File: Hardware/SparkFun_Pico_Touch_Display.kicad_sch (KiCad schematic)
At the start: 41 parts, among them J1 Conn_01x20, J2 Conn_01x20, J3 Conn_02x10_SMD_RA, J4 Conn_1x21_FPC, J5 Qwiic_Vertical, J6 microSD, Q1 RE1C002UNTCL, SW1 SMD_4.6x2.8mm_h2.5mm, U1 2" LCD-TFT 240x320

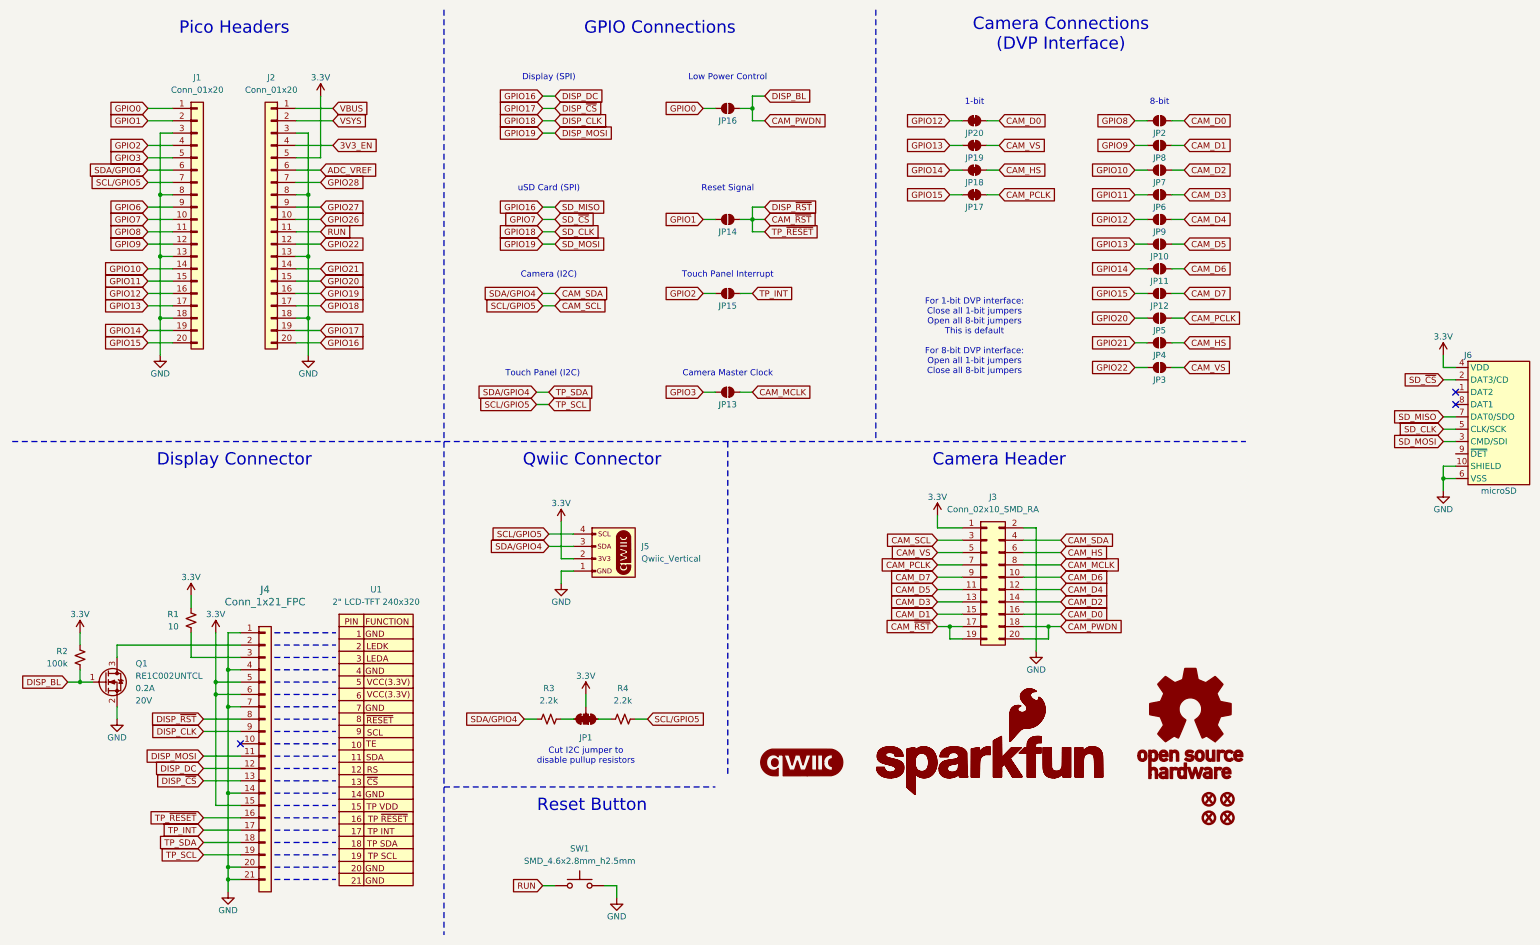
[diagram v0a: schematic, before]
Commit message: Clean up design
Finish routing
Add power LED
Move all schematic elements inside frame
Update display 3D model
Stitch together GND pours
Add measures
Fill out sheet info
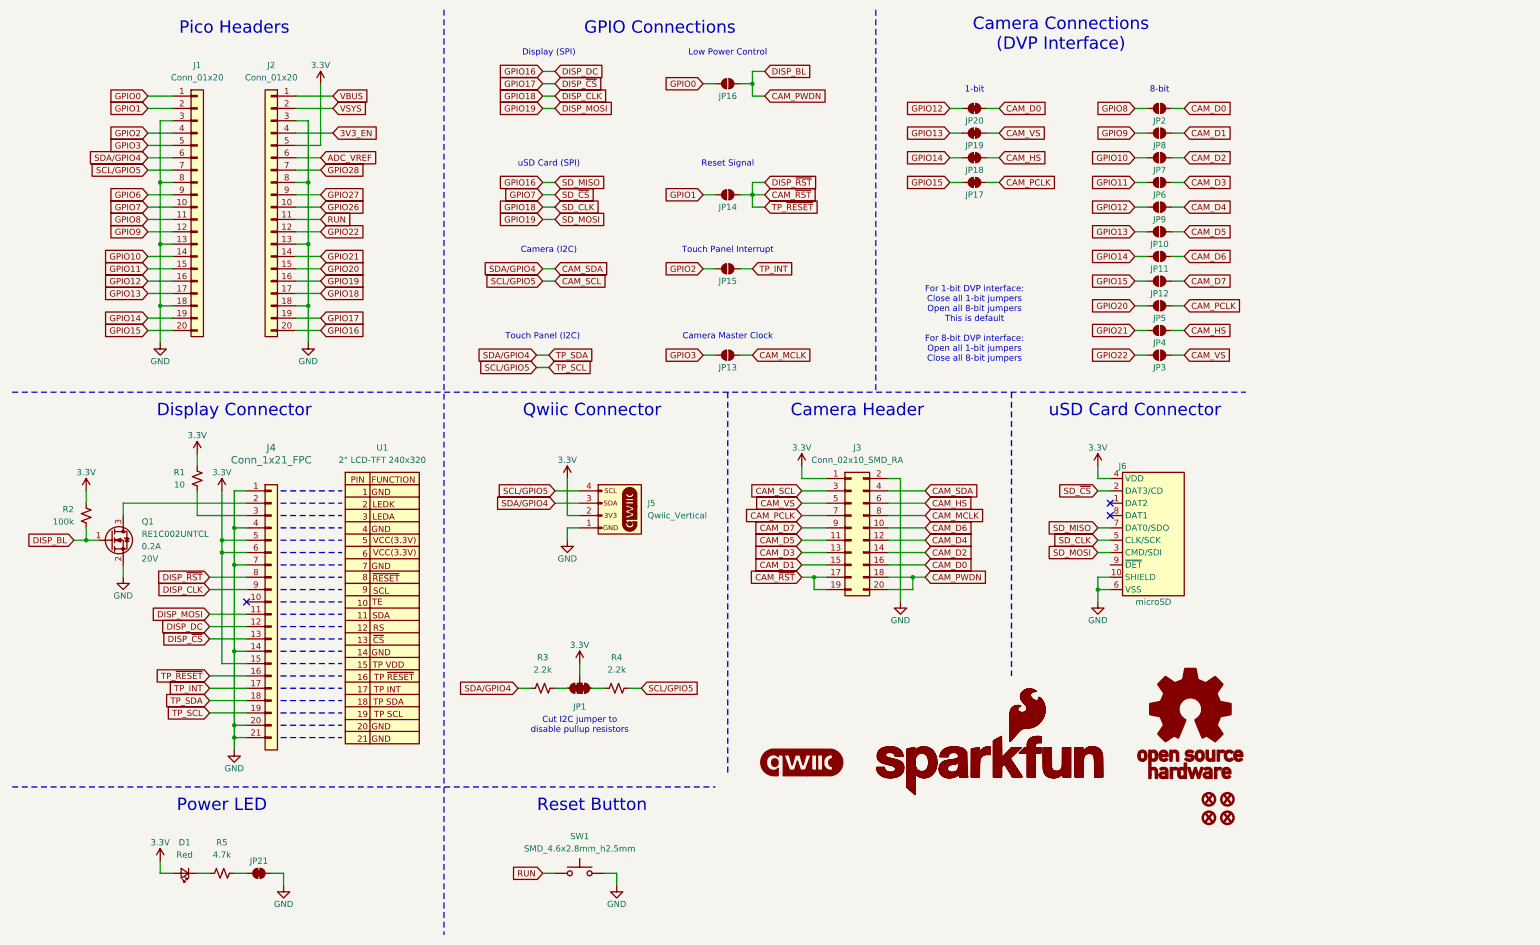
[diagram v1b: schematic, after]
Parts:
- added D1: Red, SparkFun-LED:LED_0603_1608Metric_Red, symbol SparkFun-LED:LED_Red_0603
- added JP21: ~, SparkFun-Jumper:Jumper_2_NC_Trace, symbol SparkFun-Jumper:SolderJumper_2_Bridged
- added R5: 4.7k, SparkFun-Resistor:R_0603_1608Metric, symbol SparkFun-Resistor:4.7k_0603
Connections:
- net 3.3V: now also D1.2 (A)
- net GND: now also JP21.2 (B)
- new net: D1.1 (K), R5.2
- new net: JP21.1 (A), R5.1
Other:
- note added: "Power LED"
- note added: "uSD Card Connector"
- company: SparkFun -> SparkFunElectronics
- title: SparkFun Product (Qwiic) -> SparkFun Pico Touch Display
- moved on the sheet: J1, J2, J3, J4, J5, J6, JP1, JP10, JP11, JP12, JP13, JP14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

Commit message: Design review updates
Rename jumpers to match silk
Nudge traces to provide more isolation of I2C traces
Add 10uF capacitor for uSD card
Fix acid trap
Rename MISO/MOSI to POCI/PICO
Increase 3.3V trace width
Change to 2 layer
Update ordering notes
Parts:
- added C1: 10uF, SparkFun-Capacitor:C_0603_1608Metric, symbol SparkFun-Capacitor:10uF_0603_6.3V_20%
- JP1: value ~ -> I2C
- JP10: value ~ -> 8-BIT-D5
- JP11: value ~ -> 8-BIT-D6
- JP12: value ~ -> 8-BIT-D7
- JP13: value ~ -> MCLK
- JP14: value ~ -> ~{RST}
- JP15: value ~ -> TP_INT
- JP16: value ~ -> LP
- JP17: value ~ -> 1-BIT-PCLK
- JP18: value ~ -> 1-BIT-HS
- JP19: value ~ -> 1-BIT-VS
- JP2: value ~ -> 8-BIT-D0
- JP20: value ~ -> 1-BIT-D0
- JP21: value ~ -> PWR
- JP3: value ~ -> 8-BIT-VS
- JP4: value ~ -> 8-BIT-HS
- JP5: value ~ -> 8-BIT-PCLK
- JP6: value ~ -> 8-BIT-D3
- JP7: value ~ -> 8-BIT-D2
- JP8: value ~ -> 8-BIT-D1
- JP9: value ~ -> 8-BIT-D4
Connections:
- net 3.3V: now also C1.1
- net GND: now also C1.2
- net DISP_MOSI renamed DISP_PICO
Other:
- note added: "Cut PWR jumper to disable power LED"
- moved on the sheet: J6

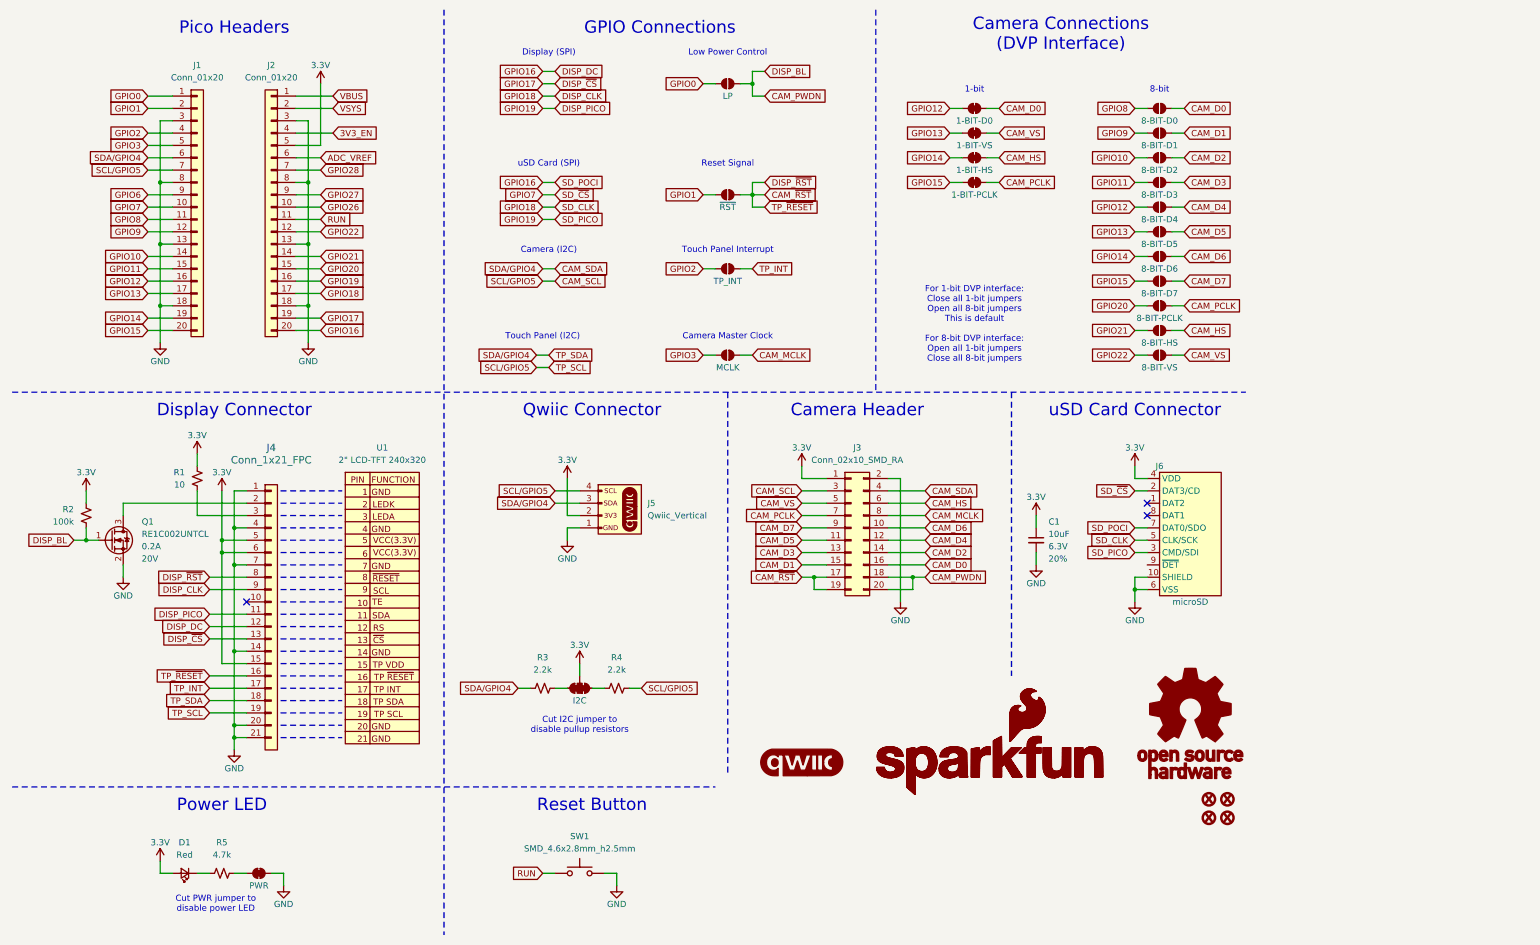
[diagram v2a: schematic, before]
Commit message: Design review updates
Change to 4 layer
Add GPIO expander for control signals
Connect uSD detection pin
Fix typo in company name on schematic
Update datahseet link for 21-pin FPC connector
Update KiCad libraries
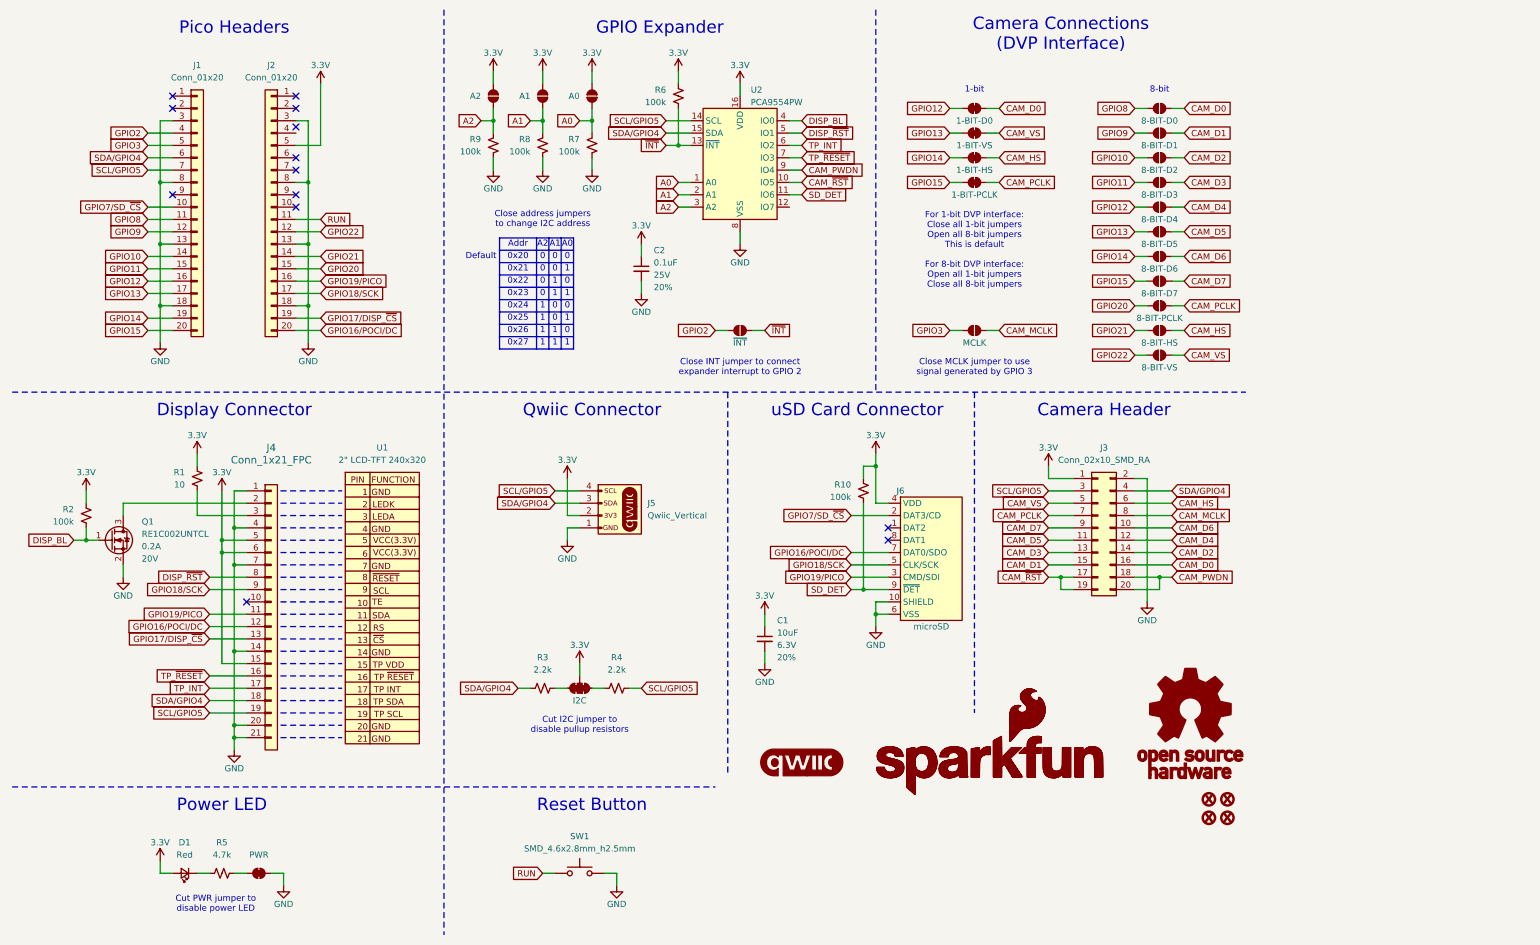
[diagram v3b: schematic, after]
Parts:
- added C2: 0.1uF, SparkFun-Capacitor:C_0603_1608Metric, symbol SparkFun-Capacitor:0.1uF_0603_25V_20%
- added JP22: ~{INT}, SparkFun-Jumper:Jumper_2_NO, symbol SparkFun-Jumper:SolderJumper_2_Open
- added R10, R6, R7, R8, R9: 100k, SparkFun-Resistor:R_0603_1608Metric, symbol SparkFun-Resistor:100k_0603
- added U2: PCA9554PW, SparkFun-Semiconductor-Standard:TSSOP-16_4.4x5mm_P0.65mm, symbol SparkFun-IC-Special-Function:PCA9554PW
- JP14: value ~{RST} -> A0
- JP15: value TP_INT -> A1
- JP16: value LP -> A2
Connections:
- net 3.3V: now also JP14.2 (B), JP15.2 (B), JP16.2 (B), C2.1, R10.2, R6.2, U2.16 (VDD)
- net CAM_PWDN: now also U2.9 (IO4); no longer JP16.1 (A), Q1.1 (G), R2.1
- net CAM_~{RST}: now also U2.10 (IO5); no longer J4.16 (Pin_16), J4.8 (Pin_8), JP14.1 (A)
- net GND: now also C2.2, R7.1, R8.1, R9.1, U2.8 (VSS)
- net GPIO2: now also JP22.2 (B); no longer JP15.2 (B)
- net TP_INT: now also U2.6 (IO2); no longer JP15.1 (A)
- net SD_DET: now reaches J6.9 (~{DET})
- net SD_DET: now also R10.1, U2.11 (IO6)
- net 3V3_EN: no longer names the net of J2.4 (Pin_4)
- net ADC_VREF: no longer names the net of J2.6 (Pin_6)
- net CAM_SCL renamed SCL/GPIO5
- net SCL/GPIO5: now also U2.14 (SCL)
- net CAM_SDA renamed SDA/GPIO4
- net SDA/GPIO4: now also U2.15 (SDA)
- net DISP_CLK renamed GPIO18/SCK
- net DISP_DC renamed GPIO16/POCI/DC
- net DISP_PICO renamed GPIO19/PICO
- net DISP_~{CS} renamed GPIO17/DISP_~{CS}
- net GPIO0: no longer names the net of J1.1 (Pin_1)
- net GPIO0: no longer JP16.2 (B)
- net GPIO1: no longer names the net of J1.2 (Pin_2)
- net GPIO1: no longer JP14.2 (B)
- net GPIO26: no longer names the net of J2.10 (Pin_10)
- net GPIO27: no longer names the net of J2.9 (Pin_9)
- net GPIO28: no longer names the net of J2.7 (Pin_7)
- net GPIO6: no longer names the net of J1.9 (Pin_9)
- net GPIO7 renamed GPIO7/SD_~{CS}
- net VBUS: no longer names the net of J2.1 (Pin_1)
- net VSYS: no longer names the net of J2.2 (Pin_2)
- new net A0: JP14.1 (A), R7.2, U2.1 (A0)
- new net A1: JP15.1 (A), R8.2, U2.2 (A1)
- new net A2: JP16.1 (A), R9.2, U2.3 (A2)
- new net DISP_BL: Q1.1 (G), R2.1, U2.4 (IO0)
- new net DISP_~{RST}: J4.8 (Pin_8), U2.5 (IO1)
- new net TP_~{RESET}: J4.16 (Pin_16), U2.7 (IO3)
- new net ~{INT}: JP22.1 (A), R6.1, U2.13 (~{INT})
- no-connect marks 3 -> 13
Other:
- note added: "0"
- note added: "0x20"
- note added: "0x21"
- note added: "0x22"
- note added: "0x23"
- note added: "0x24"
- note added: "0x25"
- note added: "0x26"
- note added: "0x27"
- note added: "1"
- note added: "A0"
- note added: "A1"
- note added: "A2"
- note added: "Addr"
- note added: "Close INT jumper to connect expander interrupt to GPIO 2"
- note added: "Close MCLK jumper to use signal generated by GPIO 3"
- note added: "Close address jumpers to change I2C address"
- note added: "Default"
- note added: "GPIO Expander"
- note removed: "Camera (I2C)"
- note removed: "Camera Master Clock"
- note removed: "Display (SPI)"
- note removed: "GPIO Connections"
- note removed: "Low Power Control"
- note removed: "Reset Signal"
- note removed: "Touch Panel (I2C)"
- note removed: "Touch Panel Interrupt"
- note removed: "uSD Card (SPI)"
- company: SparkFunElectronics -> SparkFun Electronics
- moved on the sheet: C1, J3, J6

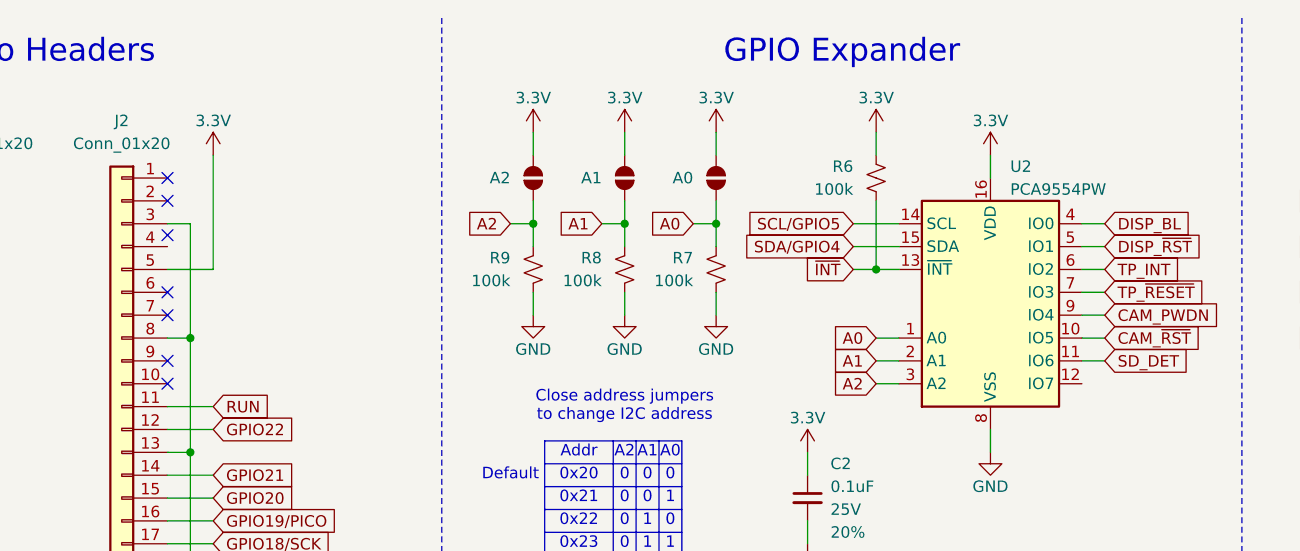
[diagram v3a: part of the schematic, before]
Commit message: Design review updates
Fix NC flags on headers and GPIO expander
Change In2.Cu to 3.3V instead of GND
Fix MOSFET datasheet link
Move Qwiic silk
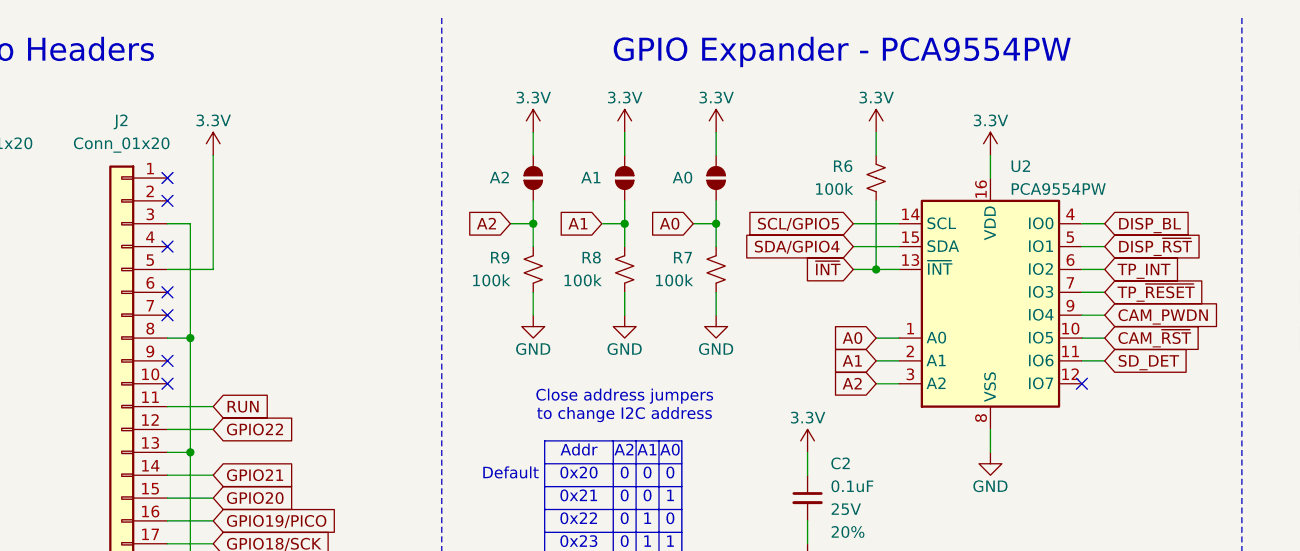
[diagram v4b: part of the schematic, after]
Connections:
- no-connect marks 13 -> 14
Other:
- note added: "GPIO Expander - PCA9554PW"
- note removed: "GPIO Expander"
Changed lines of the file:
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@@
 	)
 	(no_connect
+		(at 172.72 53.34)
+	)
+	(no_connect
 		(at 45.72 30.48)
 	)
@@
 	)
 	(no_connect
-		(at 71.12 36.83)
+		(at 71.12 38.1)
 	)
 	(wire
@@
 		)
 	)
-	(text "GPIO Expander"
+	(text "GPIO Expander - PCA9554PW"
 		(exclude_from_sim no)
 		(at 146.05 16.51 0)
@@
 			)
 		)
-		(property "Datasheet" "https://cdn.sparkfun.com/datasheets/BreakoutBoards/BSS138.pdf"
+		(property "Datasheet" "https://fscdn.rohm.com/en/products/databook/datasheet/discrete/transistor/mosfet/re1c002untcl-e.pdf"
 			(at 33.02 134.62 0)
 			(effects

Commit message: Review updates
Add 2x20 connector PROD_ID
Move R6
Swap In1.Cu and In2.Cu
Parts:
- J3: PROD_ID (none) -> CONN-25962
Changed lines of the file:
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@@
+			)
+		)
+		(property "PROD_ID" "CONN-25962"
+			(at 237.49 144.78 0)
+			(effects
+				(font
+					(size 1.27 1.27)
+				)
+				(hide yes)
 			)
 		)

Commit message: Add missing PROD_ID values
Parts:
- J4: PROD_ID (none) -> CONN-25963
- U1: PROD_ID (none) -> LCD-25764
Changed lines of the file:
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@@
+			)
+		)
+		(property "PROD_ID" "CONN-25963"
+			(at 66.04 181.61 0)
+			(effects
+				(font
+					(size 1.27 1.27)
+				)
+				(hide yes)
 			)
 		)
@@
 			(effects
 				(font
+					(size 1.27 1.27)
+				)
+				(hide yes)
+			)
+		)
+		(property "PROD_ID" "LCD-25764"
+			(at 88.9 177.8 0)
+			(effects
+				(font
